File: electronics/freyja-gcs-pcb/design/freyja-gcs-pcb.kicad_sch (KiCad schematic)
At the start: 42 parts, among them J1 JST SR, J2 GT-USB-7010ASV, J8 JST SH, J9 JST SH, SW1 SW_SPST, SW2 SW_SPST, U1 SN65HVD232DR, U2 STM32U575RGTx, Y1 48MHz, Y2 32768Hz

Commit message: raspberry pi header
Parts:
- added C45, C46, C47, C48: 22u, EasyEDA:C1210, symbol Device:C_Small
- added H1, H2, H3, H4: M2.5 12mm, EasyEDA:SMTSO25, symbol Mechanical:MountingHole_Pad
- added J10: 2x20F, symbol Connector_Generic:Conn_02x20_Odd_Even
- added R75, R76, R77, R78: 10k, symbol Device:R
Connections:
- net GND: now also C45.2, C46.2, C47.2, C48.2, J10.14 (Pin_14), J10.20 (Pin_20), J10.25 (Pin_25), J10.30 (Pin_30), J10.34 (Pin_34), J10.39 (Pin_39), J10.6 (Pin_6), J10.9 (Pin_9), R75.2, R76.2, R77.2, R78.2
- new net: H4.1, R78.1
- new net: H3.1, R77.1
- new net: H2.1, R76.1
- new net: H1.1, R75.1
- new net +5V: C45.1, C46.1, C47.1, C48.1, J10.2 (Pin_2), J10.4 (Pin_4)
- no-connect marks 5 -> 35
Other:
- note added: "RPI HEADER"
- note added: "RPI NUTS"

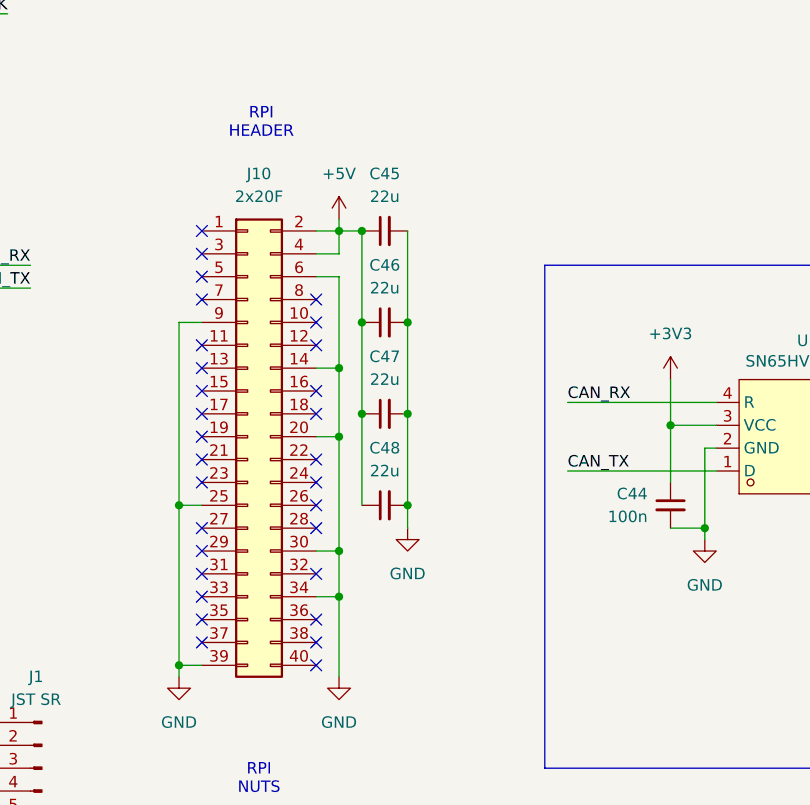
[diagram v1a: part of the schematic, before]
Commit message: more esd diodes
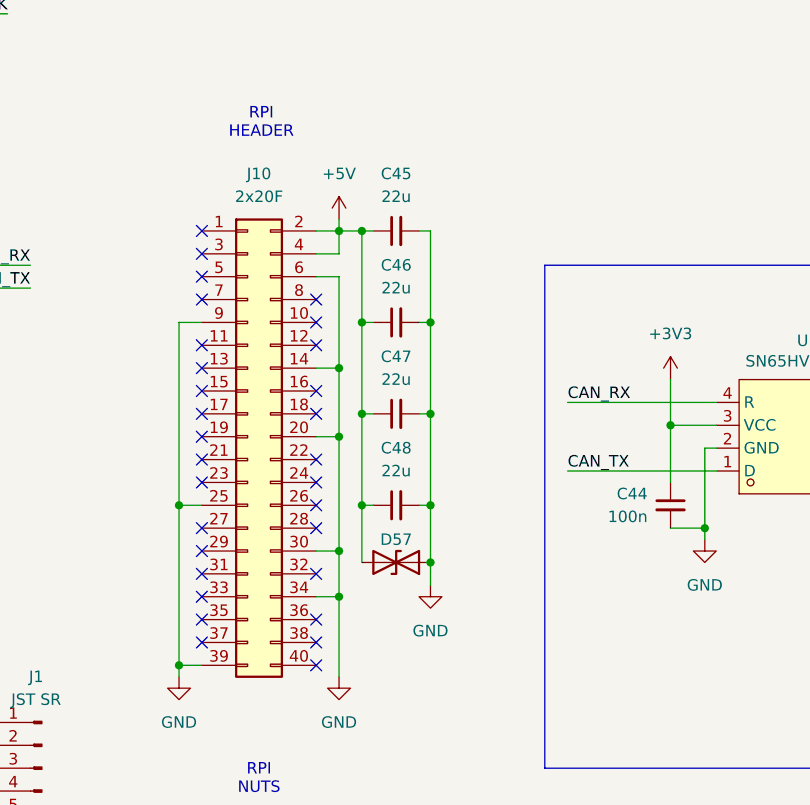
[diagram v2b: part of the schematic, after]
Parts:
- added D57: 0603ESDA-05N, Diode_SMD:D_0603_1608Metric_Pad1.05x0.95mm_HandSolder, symbol Device:D_TVS
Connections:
- net +5V: now also D57.2 (A2)
- net GND: now also D57.1 (A1)
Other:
- moved on the sheet: C45, C46, C47, C48

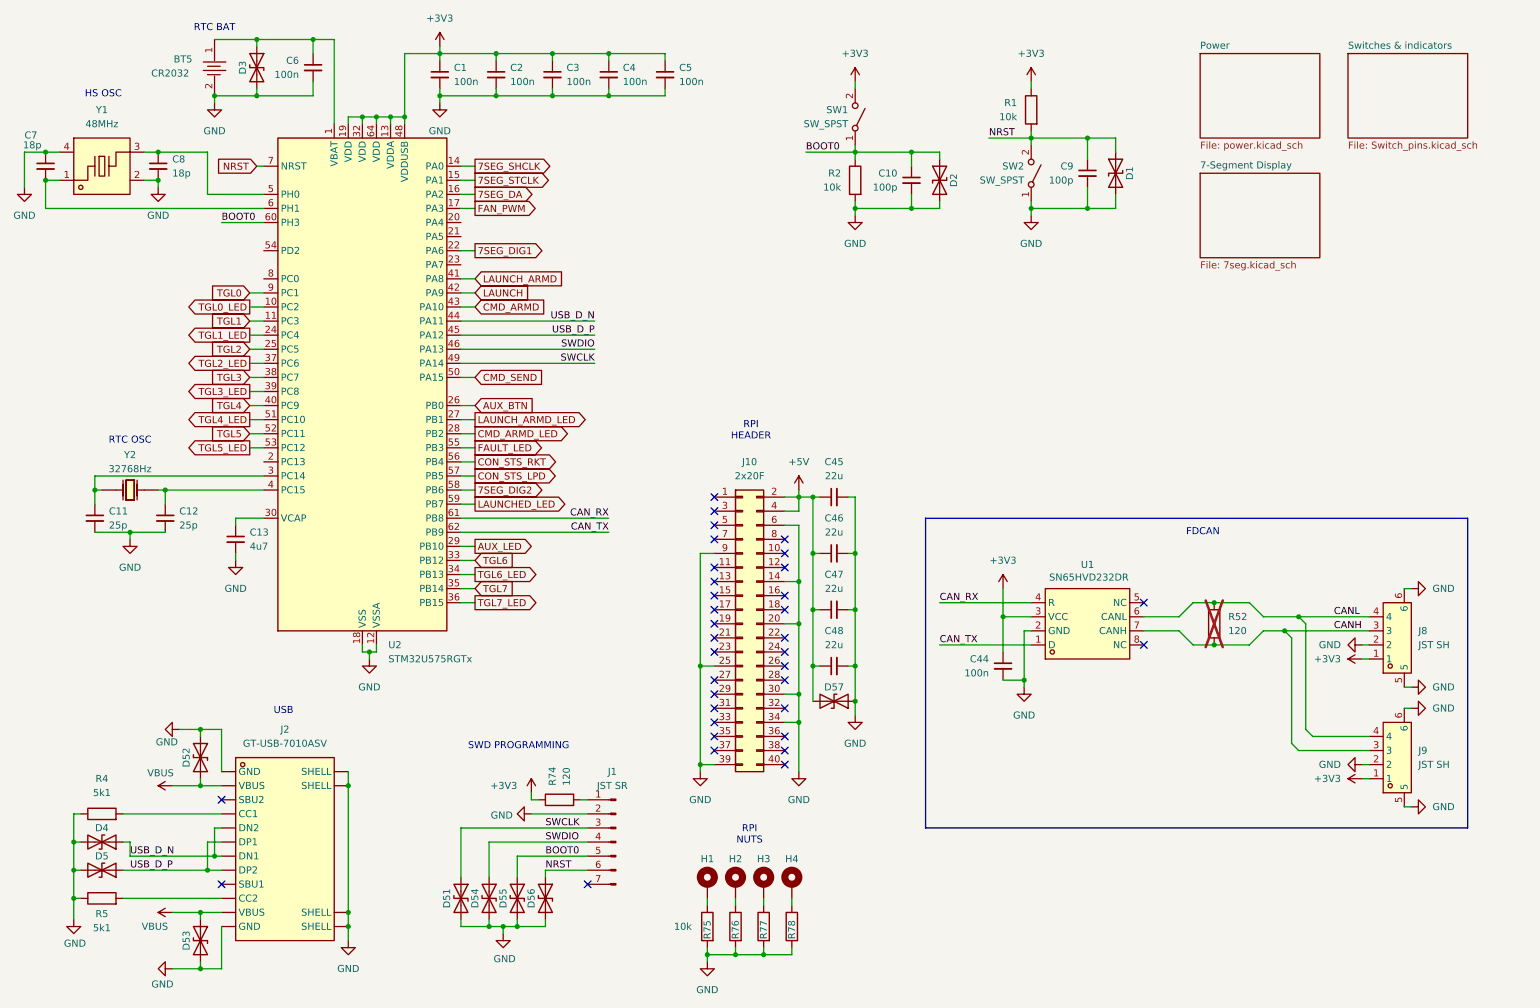
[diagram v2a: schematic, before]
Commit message: reset designators
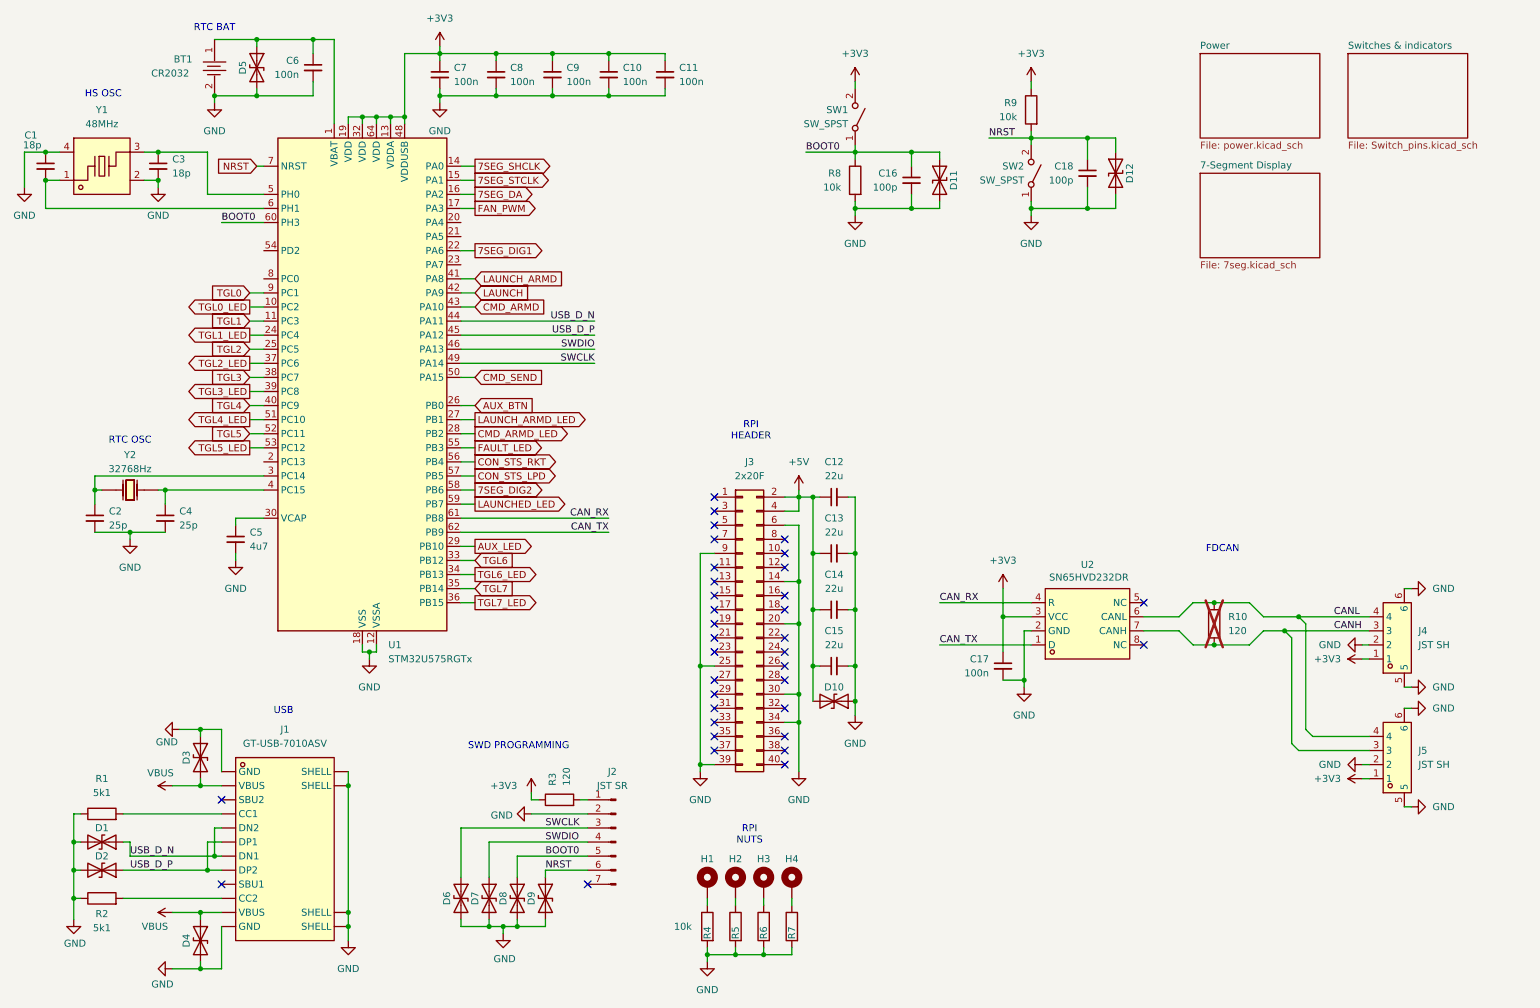
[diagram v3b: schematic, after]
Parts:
- H1, H2, H3, H4: now in the parts list
- R10: renamed from R52; now left out of the parts list
- renumbered BT5 to BT1, C7 to C1, C4 to C10, C5 to C11, C45 to C12, C46 to C13, C47 to C14, C48 to C15, C10 to C16, C44 to C17, C9 to C18, C11 to C2, C8 to C3, C12 to C4, C13 to C5, C1 to C7, C2 to C8, C3 to C9, D4 to D1, D57 to D10, D2 to D11, D1 to D12, D5 to D2, D52 to D3, D53 to D4, D3 to D5, D51 to D6, D54 to D7, D55 to D8, D56 to D9, J2 to J1, J1 to J2, J10 to J3, J8 to J4, J9 to J5, R4 to R1, R5 to R2, R74 to R3, R75 to R4, R76 to R5, R77 to R6, R78 to R7, R2 to R8, R1 to R9, U2 to U1, U1 to U2

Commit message: add jumpers so that can power on cna port can be disconnected
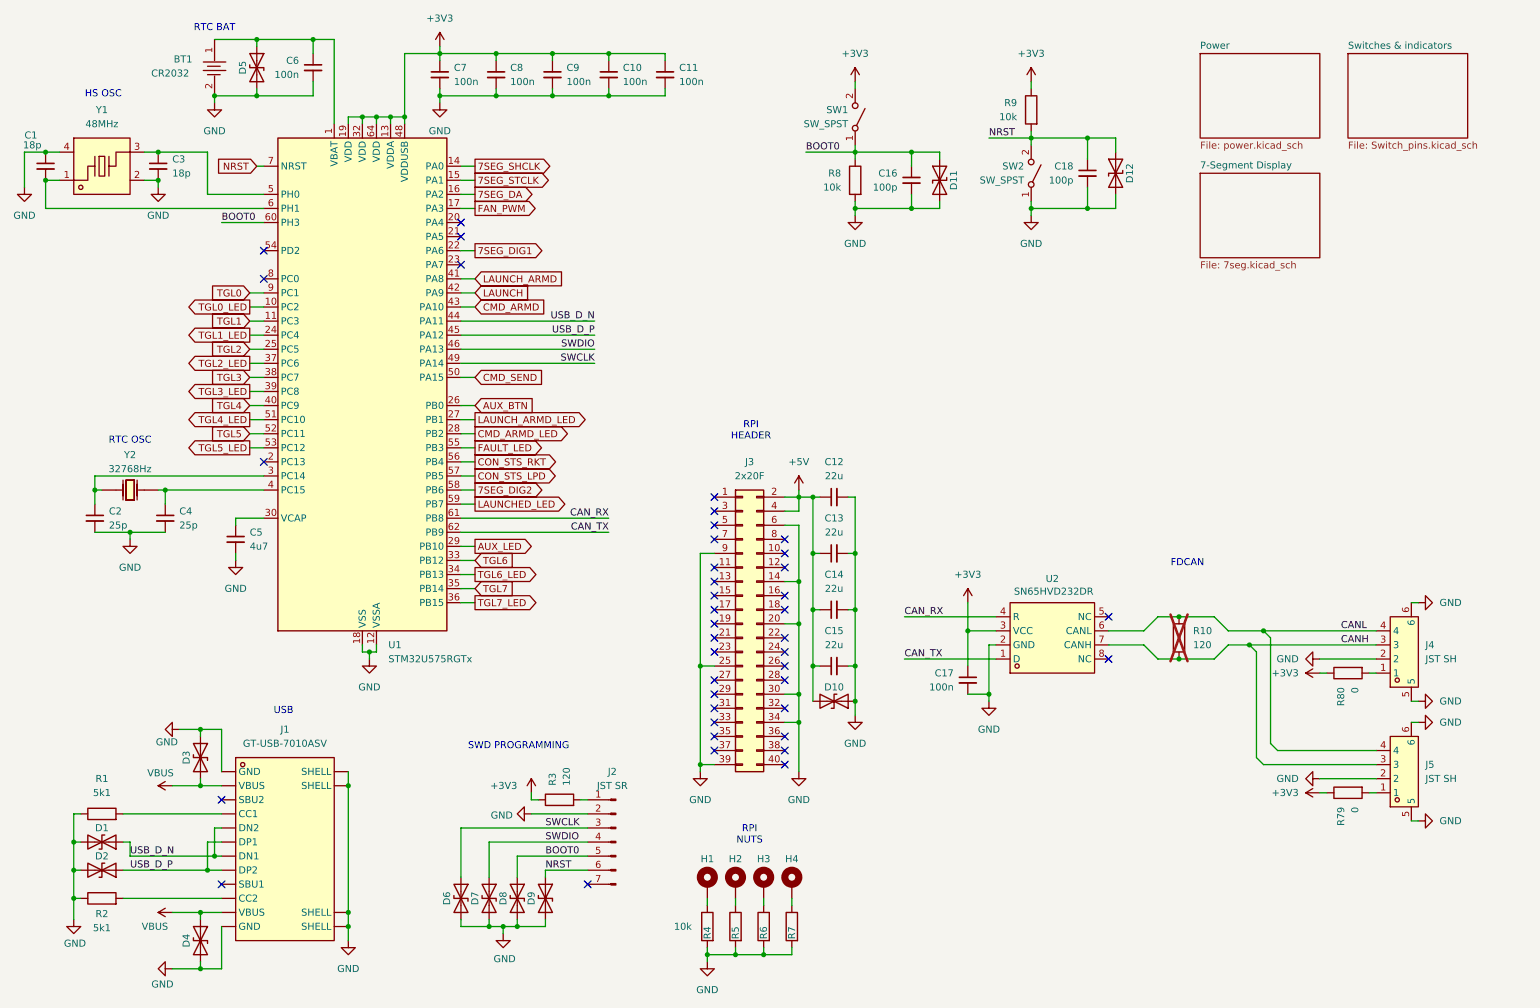
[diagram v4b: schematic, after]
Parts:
- added R79, R80: 0, symbol Device:R
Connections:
- net +3V3: now also R79.1, R80.1; no longer J4.1, J5.1
- new net: J5.1, R79.2
- new net: J4.1, R80.2
- no-connect marks 35 -> 41
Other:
- moved on the sheet: C17, J4, J5, R10, U2

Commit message: footprint and lcsc part for all components
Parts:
- C1, C3: footprint (none) -> Capacitor_SMD:C_0603_1608Metric; LCSC Part (none) -> C5137620
- C10, C11, C17, C6, C7, C8, C9: footprint (none) -> Capacitor_SMD:C_0603_1608Metric; LCSC Part (none) -> C2762593
- C16, C18: footprint (none) -> Capacitor_SMD:C_0603_1608Metric; LCSC Part (none) -> C14665
- C2, C4: footprint (none) -> Capacitor_SMD:C_0603_1608Metric; LCSC Part (none) -> C282067
- C5: footprint (none) -> Capacitor_SMD:C_0603_1608Metric; LCSC Part (none) -> C19666
- J3: footprint (none) -> Connector_PinSocket_2.54mm:PinSocket_2x20_P2.54mm_Vertical
- R1, R10, R2, R3: footprint (none) -> Resistor_SMD:R_0603_1608Metric; LCSC Part (none) -> C23186
- R4, R5, R6, R7, R8, R9: footprint (none) -> Resistor_SMD:R_0603_1608Metric; LCSC Part (none) -> C98220
- R79, R80: footprint (none) -> Resistor_SMD:R_0603_1608Metric; LCSC Part (none) -> C2906974
- SW1, SW2: footprint (none) -> Button_Switch_SMD:SW_SPST_PTS647_Sx38; LCSC Part (none) -> C127509
- U1: LCSC Part (none) -> C5270980

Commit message: 3d model improvement
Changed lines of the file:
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@@
 		(pin "4"
 		)
-		(pin "7"
+		(pin "MP"
 		)
 		(pin "3"

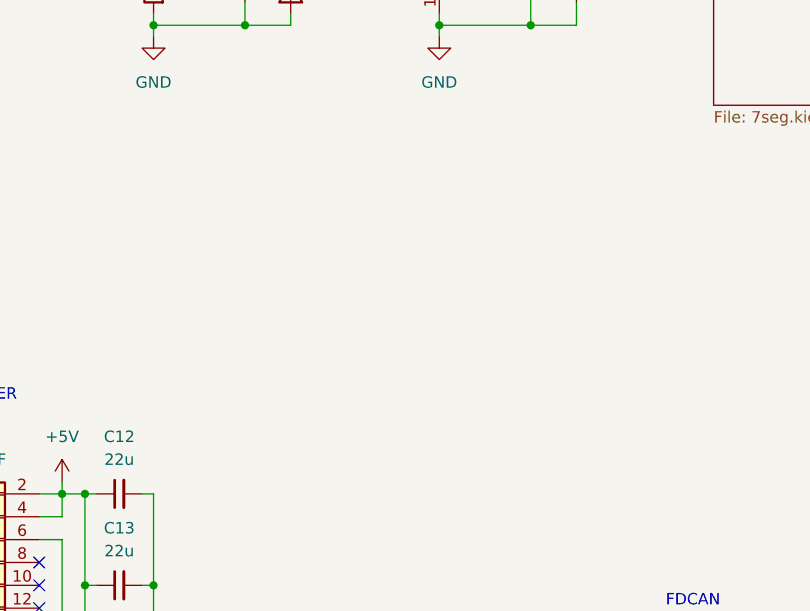
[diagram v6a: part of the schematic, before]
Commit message: Updated schematic with the board mounting
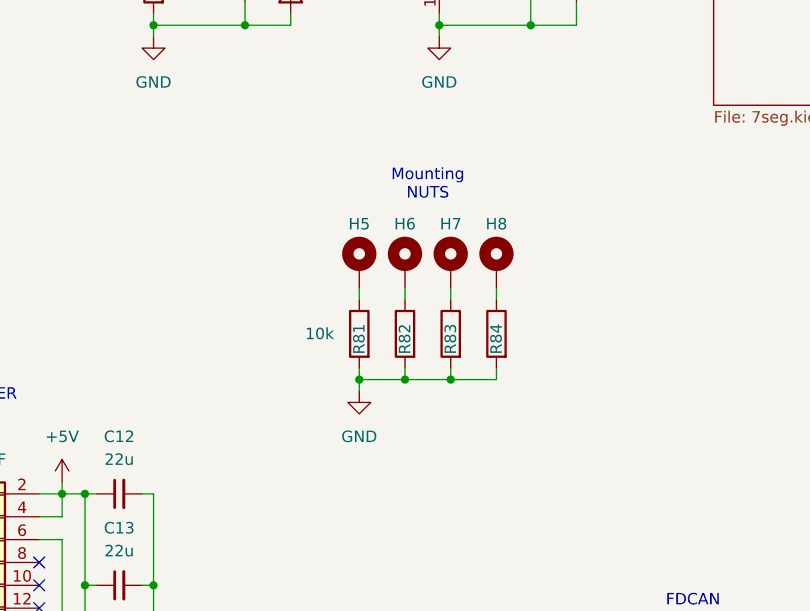
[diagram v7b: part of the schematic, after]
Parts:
- added H5, H6, H7, H8: M2.5 12mm, EasyEDA:SMTSO25, symbol Mechanical:MountingHole_Pad
- added R81, R82, R83, R84: 10k, Resistor_SMD:R_0603_1608Metric, symbol Device:R
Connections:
- net GND: now also R81.2, R82.2, R83.2, R84.2
- new net: H8.1, R84.1
- new net: H7.1, R83.1
- new net: H5.1, R81.1
- new net: H6.1, R82.1
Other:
- note added: "Mounting NUTS"

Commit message: power layout wip
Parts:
- added H10, H9: M2.5 12mm, EasyEDA:SMTSO25, symbol Mechanical:MountingHole_Pad
- added R85, R86: 10k, Resistor_SMD:R_0603_1608Metric, symbol Device:R
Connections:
- net GND: now also R85.2, R86.2
- new net: H9.1, R85.1
- new net: H10.1, R86.1
